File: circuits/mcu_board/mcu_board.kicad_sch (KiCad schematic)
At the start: 79 parts, among them J1 USB_B_Micro, J2 Conn_01x13_Pin, J3 Conn_01x04_Pin, J4 Conn_01x03_Socket, SW1 SW_Push, SW10 SW_Push, SW11 SW_Push, SW12 SW_Push, SW13 SW_Push, SW2 SW_Push, SW3 SW_Push, SW4 SW_Push, SW5 SW_Push, SW6 SW_Push, SW7 SW_Push, SW8 SW_Push, SW9 SW_Push, U1 AMS1117-3.3, U2 74HC165, U3 74HC165, U4 STM32F302CCTx, Y1 8MHz

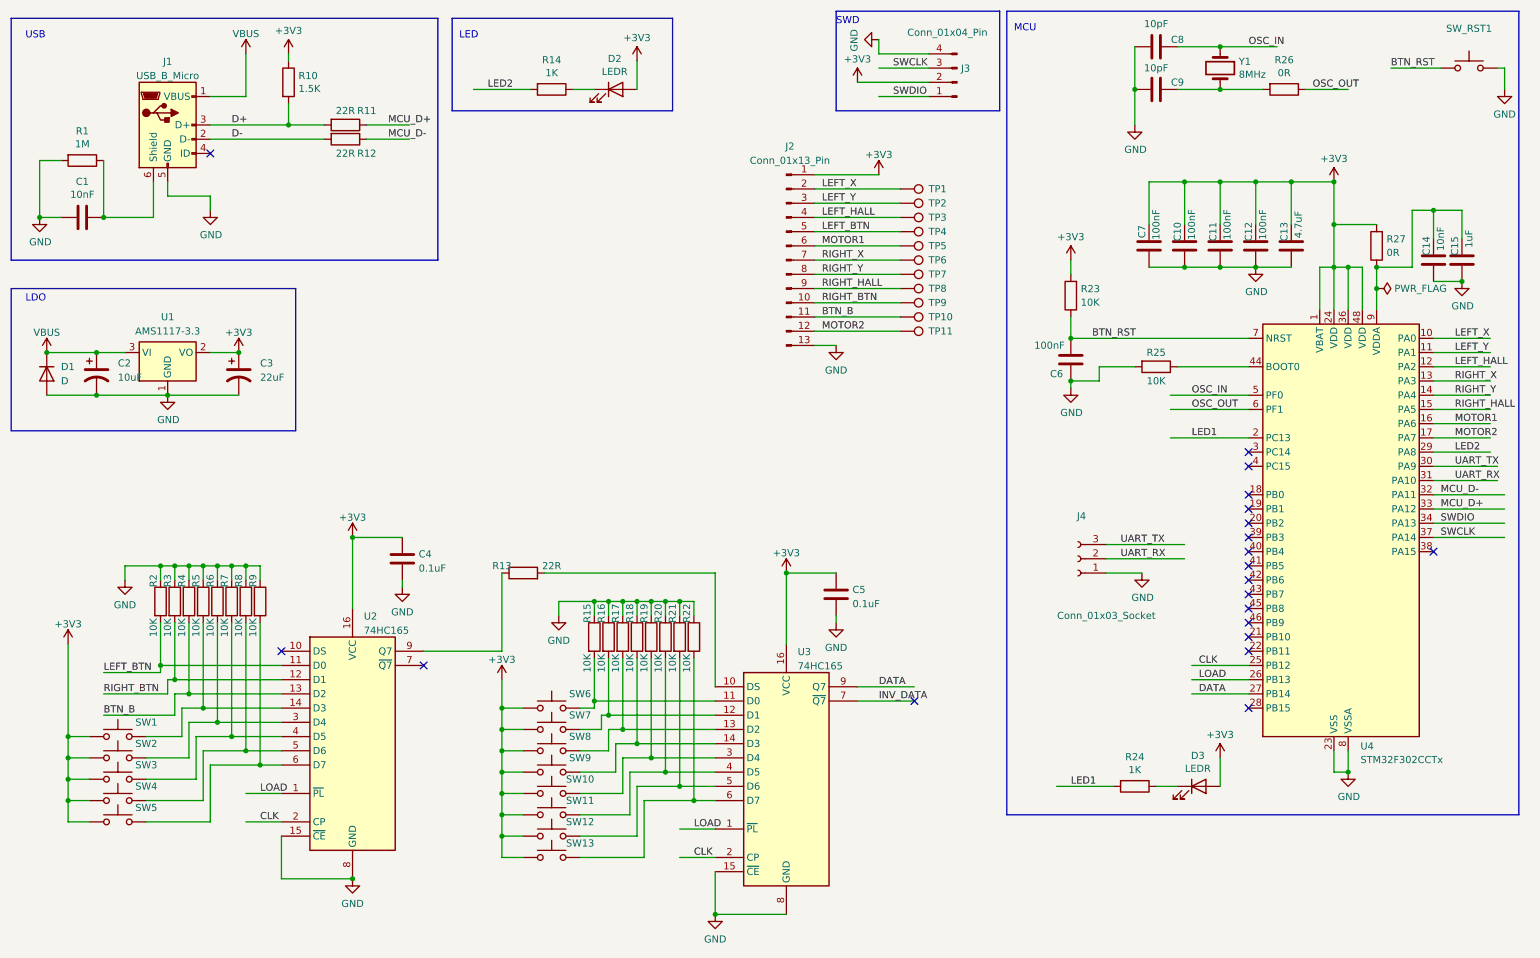
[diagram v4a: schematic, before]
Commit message: 更新mcu板原理图,改晶振封装
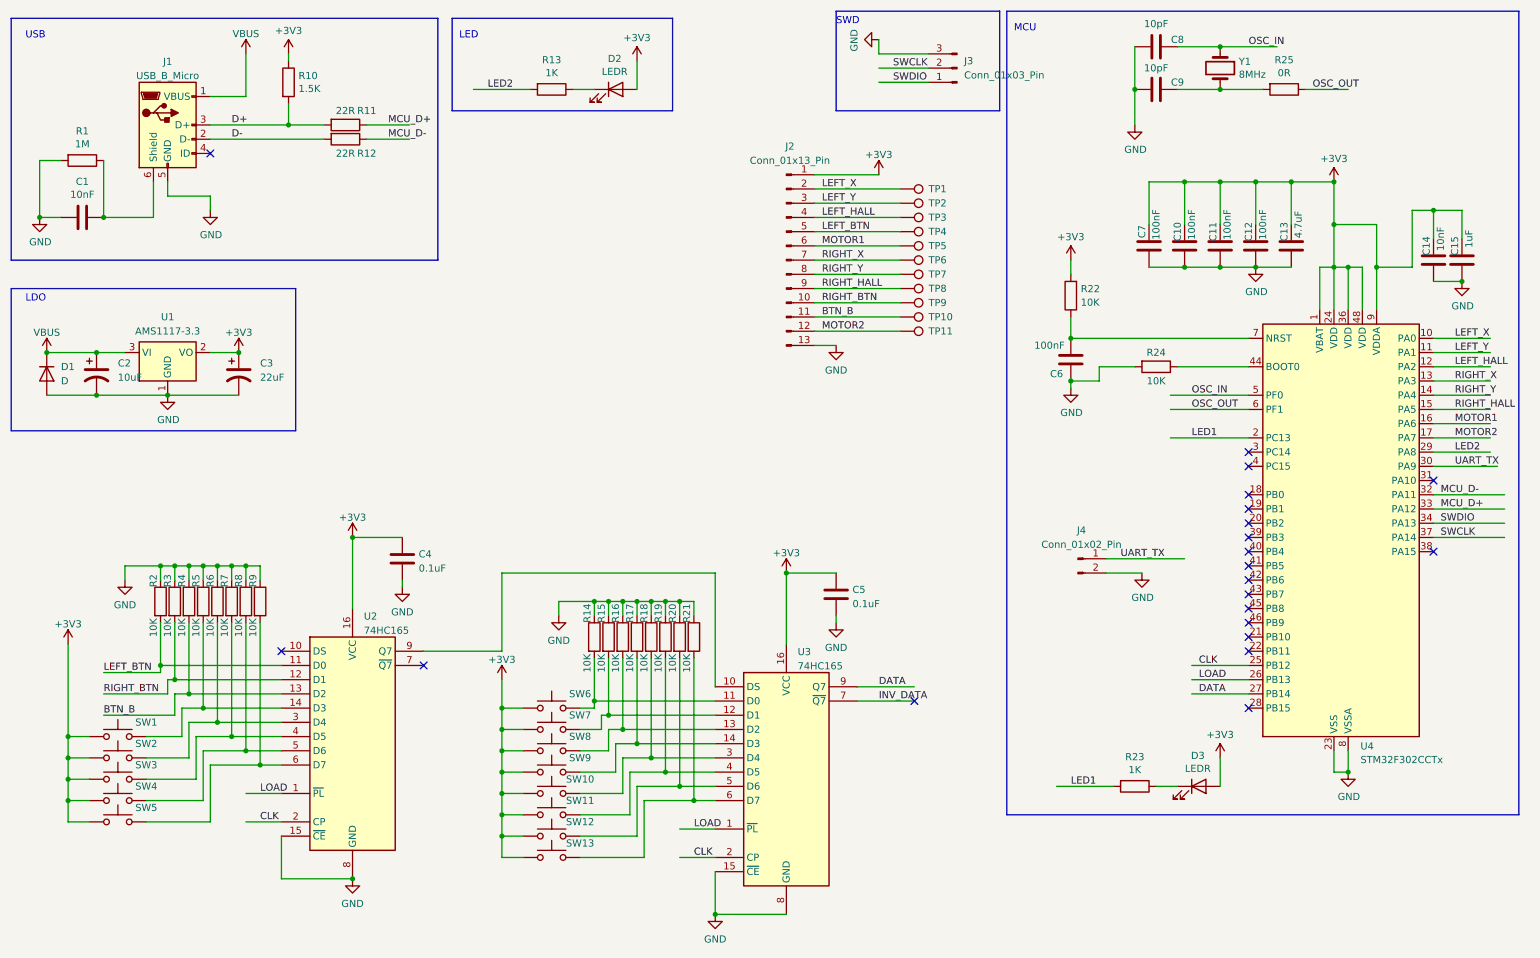
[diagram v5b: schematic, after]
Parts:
- removed J3: Conn_01x04_Pin, Connector_PinSocket_2.54mm:PinSocket_1x04_P2.54mm_Vertical, symbol Connector:Conn_01x04_Pin
- removed J4: Conn_01x03_Socket, Connector_PinSocket_2.54mm:PinSocket_1x03_P2.54mm_Vertical, symbol Connector:Conn_01x03_Socket
- removed R13: 22R, Resistor_SMD:R_0805_2012Metric_Pad1.20x1.40mm_HandSolder, symbol Device:R
- removed R27: 0R, Resistor_SMD:R_0805_2012Metric_Pad1.20x1.40mm_HandSolder, symbol Device:R
- removed SW_RST1: SW_RST, Button_Switch_SMD:SW_Push_1P1T_NO_6x6mm_H9.5mm, symbol Switch:SW_Push
- added J3: Conn_01x03_Pin, Connector_PinHeader_2.54mm:PinHeader_1x03_P2.54mm_Vertical, symbol Connector:Conn_01x03_Pin
- added J4: Conn_01x02_Pin, Connector_PinHeader_2.54mm:PinHeader_1x02_P2.54mm_Vertical, symbol Connector:Conn_01x02_Pin
- Y1: footprint Crystal:Crystal_SMD_HC49-SD_HandSoldering -> Crystal:Crystal_SMD_5032-2Pin_5.0x3.2mm_HandSoldering
- renumbered R14 to R13, R15 to R14, R16 to R15, R17 to R16, R18 to R17, R19 to R18, R20 to R19, R21 to R20, R22 to R21, R23 to R22, R24 to R23, R25 to R24, R26 to R25
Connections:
- net +3V3: now also C14.1, C15.1, U4.9 (VDDA)
- net GND: now also J3.3 (Pin_3), J4.2 (Pin_2)
- net SWCLK: now also J3.2 (Pin_2)
- net SWDIO: now also J3.1 (Pin_1)
- net UART_TX: now also J4.1 (Pin_1)
- net at U3.10 (DS): now also U2.9 (Q7)
- net BTN_RST: no longer names the net of C6.1, R22.1, U4.7 (NRST)
- net UART_RX: no longer names the net of U4.31 (PA10)
- no-connect marks 20 -> 21

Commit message: mcu板极端精简电路
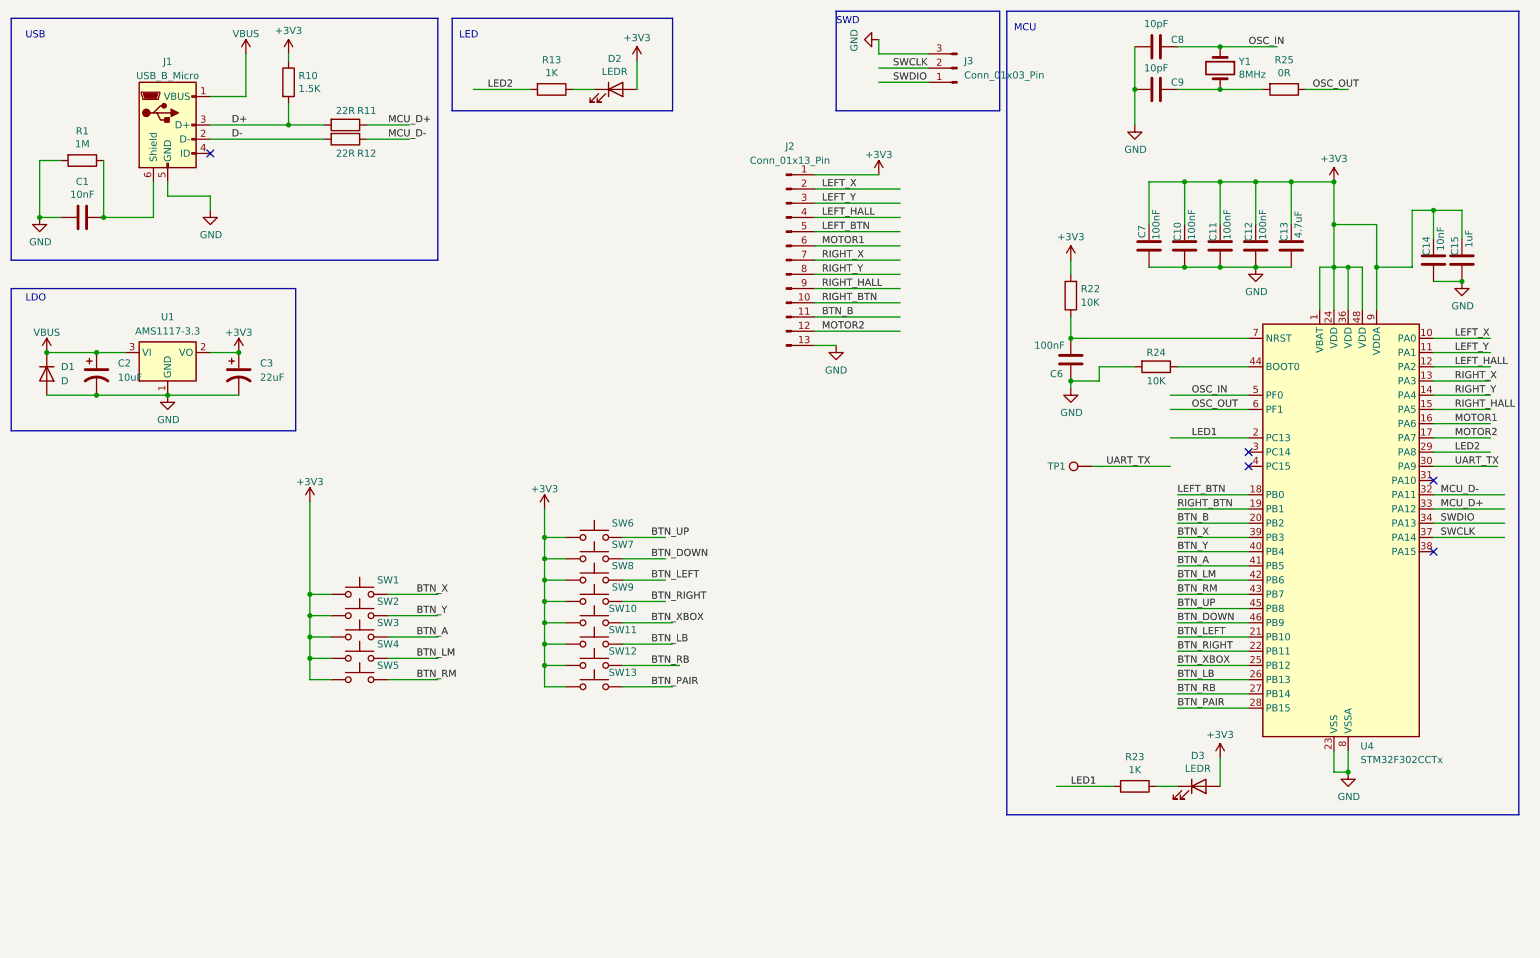
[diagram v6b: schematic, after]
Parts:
- removed C4, C5: 0.1uF, Capacitor_SMD:C_0805_2012Metric_Pad1.18x1.45mm_HandSolder, symbol Device:C
- removed J4: Conn_01x02_Pin, Connector_PinHeader_2.54mm:PinHeader_1x02_P2.54mm_Vertical, symbol Connector:Conn_01x02_Pin
- removed R14, R15, R16, R17, R18, R19, R2, R20, R21, R3, R4, R5, R6, R7, R8, R9: 10K, Resistor_SMD:R_0805_2012Metric_Pad1.20x1.40mm_HandSolder, symbol Device:R
- removed TP10, TP11, TP2, TP3, TP4, TP5, TP6, TP7, TP8, TP9: TestPoint, TestPoint:TestPoint_Pad_1.5x1.5mm, symbol Connector:TestPoint
- removed U2, U3: 74HC165, Package_SO:SOP-16_4.4x10.4mm_P1.27mm, symbol 74xx:74HC165
- TP1: footprint TestPoint:TestPoint_Pad_1.5x1.5mm -> TestPoint:TestPoint_Pad_1.0x1.0mm
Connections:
- net CLK is gone; now on net BTN_XBOX: U4.25 (PB12)
- net DATA is gone; now on net BTN_RB: U4.27 (PB14)
- net LOAD is gone; now on net BTN_LB: U4.26 (PB13)
- net BTN_B: now also U4.20 (PB2)
- net LEFT_BTN: now also U4.18 (PB0)
- net LEFT_X: no longer TP1.1
- net RIGHT_BTN: now also U4.19 (PB1)
- net UART_TX: now also TP1.1
- net BTN_PAIR: now reaches SW13.2
- net BTN_PAIR: now also U4.28 (PB15)
- net BTN_A: now reaches SW3.2
- net BTN_A: now also U4.41 (PB5)
- net BTN_Y: now reaches SW2.2
- net BTN_Y: now also U4.40 (PB4)
- net BTN_XBOX: now reaches SW10.2
- net BTN_X: now reaches SW1.2
- net BTN_X: now also U4.39 (PB3)
- net BTN_UP: now reaches SW6.2
- net BTN_UP: now also U4.45 (PB8)
- net BTN_DOWN: now reaches SW7.2
- net BTN_DOWN: now also U4.46 (PB9)
- net BTN_LEFT: now reaches SW8.2
- net BTN_LEFT: now also U4.21 (PB10)
- net BTN_RIGHT: now reaches SW9.2
- net BTN_RIGHT: now also U4.22 (PB11)
- net BTN_LB: now reaches SW11.2
- net BTN_RB: now reaches SW12.2
- net BTN_LM: now reaches SW4.2
- net BTN_LM: now also U4.42 (PB6)
- net BTN_RM: now reaches SW5.2
- net BTN_RM: now also U4.43 (PB7)
- no-connect marks 21 -> 5
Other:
- moved on the sheet: SW1, SW10, SW11, SW12, SW13, SW2, SW3, SW4, SW5, SW6, SW7, SW8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

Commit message: laytou MCU板基本完成走线
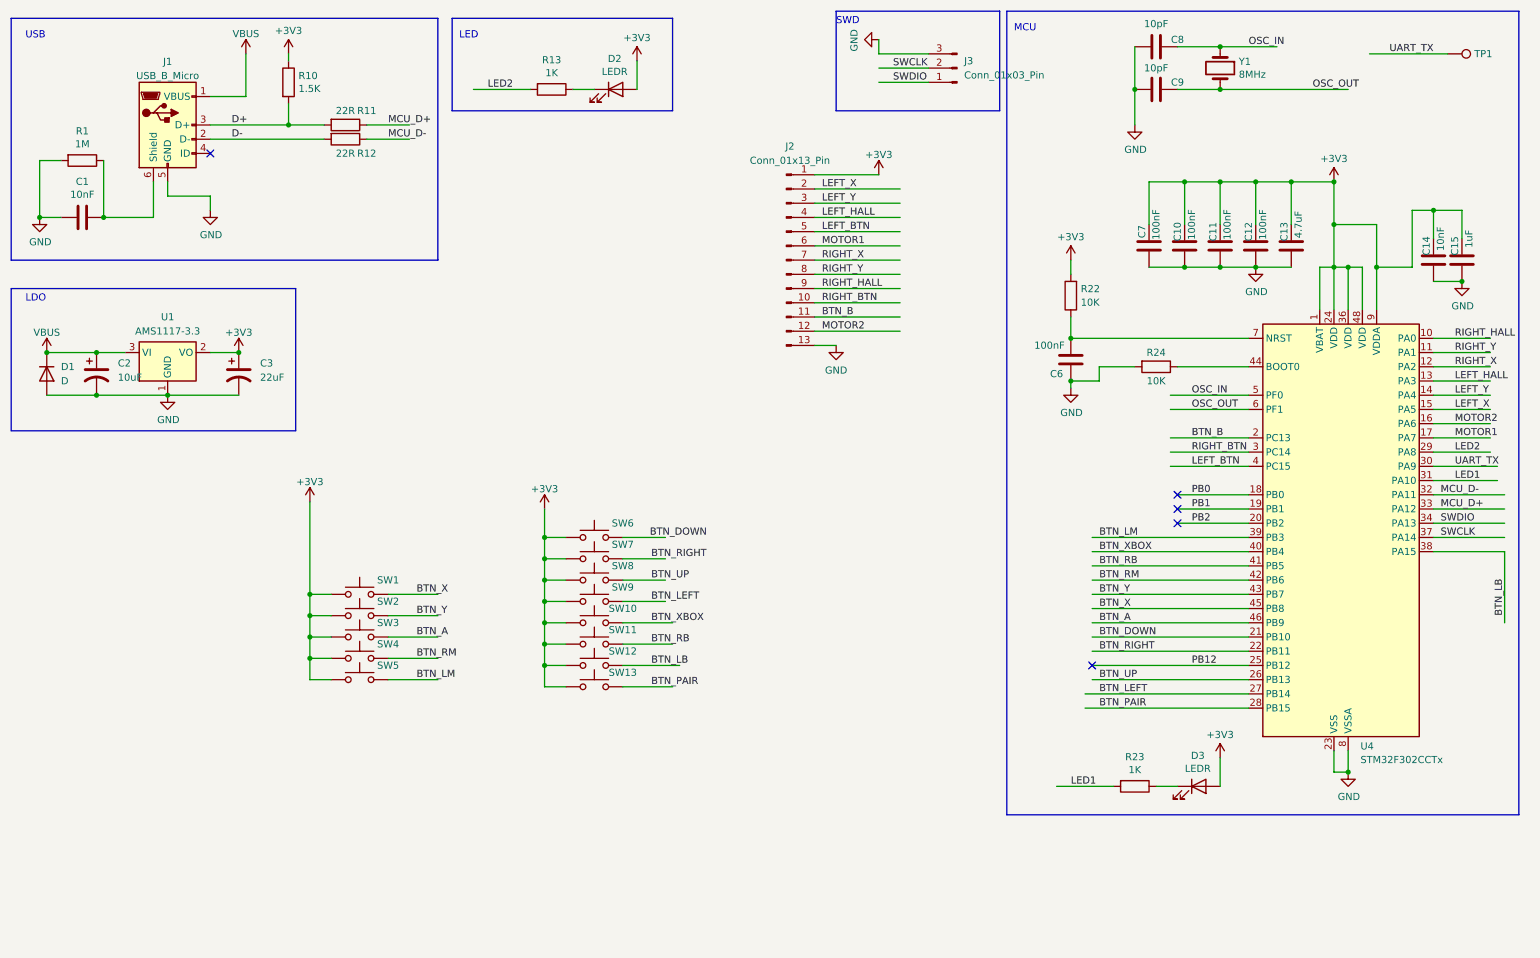
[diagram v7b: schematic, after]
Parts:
- removed R25: 0R, Resistor_SMD:R_0805_2012Metric_Pad1.20x1.40mm_HandSolder, symbol Device:R
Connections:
- net BTN_A: now also U4.46 (PB9); no longer U4.41 (PB5)
- net BTN_B: now also U4.2 (PC13); no longer U4.20 (PB2)
- net BTN_DOWN: now also SW6.2, U4.21 (PB10); no longer SW7.2, U4.46 (PB9)
- net BTN_LB: now also SW12.2, U4.38 (PA15); no longer SW11.2, U4.26 (PB13)
- net BTN_LEFT: now also SW9.2, U4.27 (PB14); no longer SW8.2, U4.21 (PB10)
- net BTN_LM: now also SW5.2, U4.39 (PB3); no longer SW4.2, U4.42 (PB6)
- net BTN_RB: now also SW11.2, U4.41 (PB5); no longer SW12.2, U4.27 (PB14)
- net BTN_RIGHT: now also SW7.2; no longer SW9.2
- net BTN_RM: now also SW4.2, U4.42 (PB6); no longer SW5.2, U4.43 (PB7)
- net BTN_UP: now also SW8.2, U4.26 (PB13); no longer SW6.2, U4.45 (PB8)
- net BTN_X: now also U4.45 (PB8); no longer U4.39 (PB3)
- net BTN_XBOX: now also U4.40 (PB4); no longer U4.25 (PB12)
- net BTN_Y: now also U4.43 (PB7); no longer U4.40 (PB4)
- net LED1: now also U4.31 (PA10); no longer U4.2 (PC13)
- net LEFT_BTN: now also U4.4 (PC15); no longer U4.18 (PB0)
- net LEFT_HALL: now also U4.13 (PA3); no longer U4.12 (PA2)
- net LEFT_X: now also U4.15 (PA5); no longer U4.10 (PA0)
- net LEFT_Y: now also U4.14 (PA4); no longer U4.11 (PA1)
- net MOTOR1: now also U4.17 (PA7); no longer U4.16 (PA6)
- net MOTOR2: now also U4.16 (PA6); no longer U4.17 (PA7)
- net OSC_OUT: now also C9.1, Y1.2
- net RIGHT_BTN: now also U4.3 (PC14); no longer U4.19 (PB1)
- net RIGHT_HALL: now also U4.10 (PA0); no longer U4.15 (PA5)
- net RIGHT_X: now also U4.12 (PA2); no longer U4.13 (PA3)
- net RIGHT_Y: now also U4.11 (PA1); no longer U4.14 (PA4)
- new net PB0: U4.18 (PB0)
- new net PB1: U4.19 (PB1)
- new net PB12: U4.25 (PB12)
- new net PB2: U4.20 (PB2)

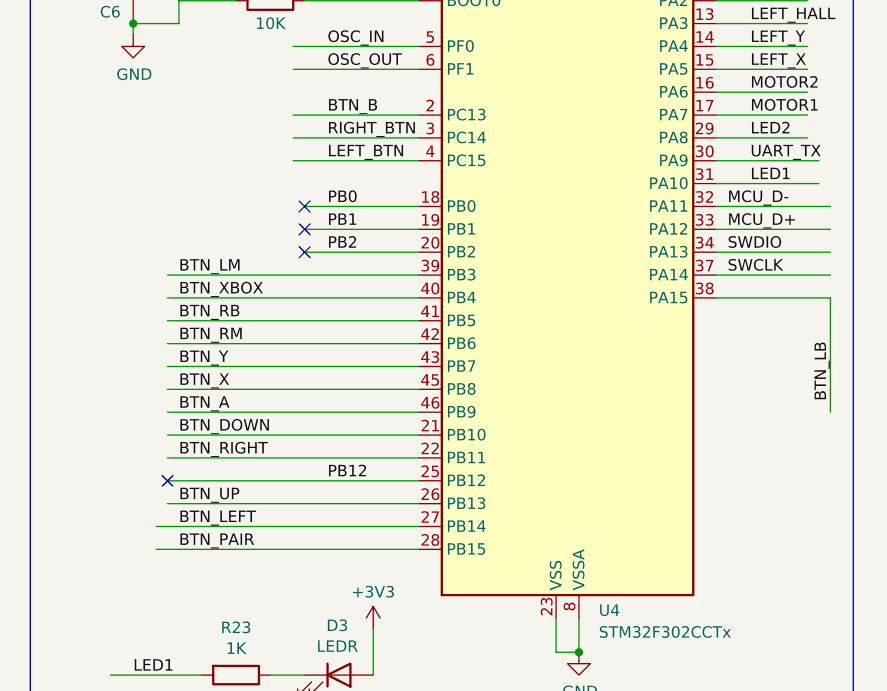
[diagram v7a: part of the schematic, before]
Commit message: 按键逻辑修改完成,未测试
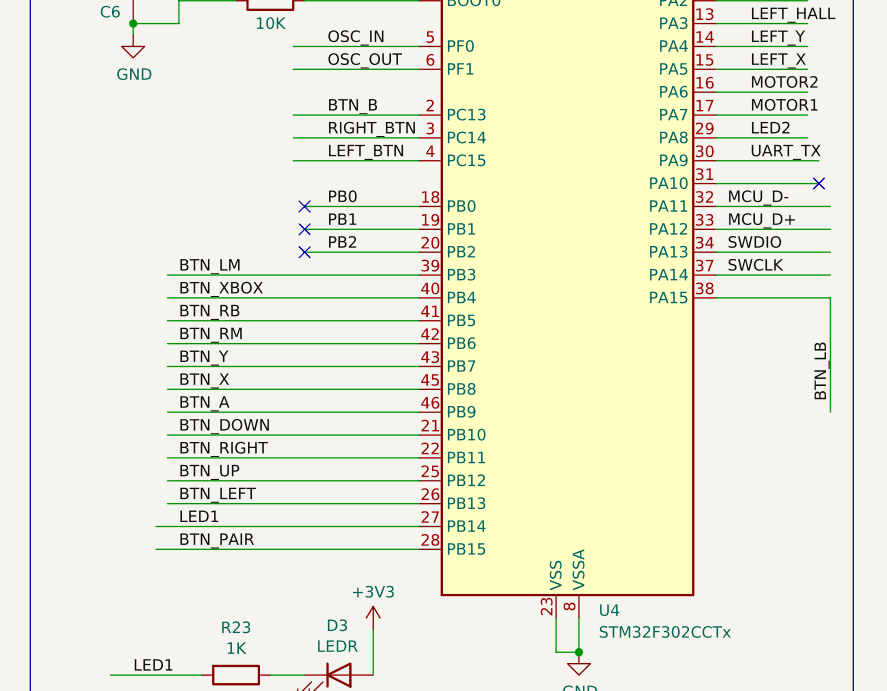
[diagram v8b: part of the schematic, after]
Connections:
- net PB12 is gone; now on net BTN_UP: U4.25 (PB12)
- net BTN_LEFT: now also U4.26 (PB13); no longer U4.27 (PB14)
- net BTN_UP: no longer U4.26 (PB13)
- net LED1: now also U4.27 (PB14); no longer U4.31 (PA10)
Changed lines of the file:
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@@
   (no_connect (at 50.8 38.1))
   (no_connect (at 223.52 99.06))
-  (no_connect (at 208.28 129.54))
   (no_connect (at 223.52 104.14))
   (no_connect (at 223.52 101.6))
+  (no_connect (at 280.67 96.52))
   (wire (pts (xy 237.49 43.18) (xy 237.49 50.8))
     (stroke (width 0) (type default))
@@
     (effects (font (size 1.27 1.27)) (justify left bottom))
   )
-  (label "BTN_LEFT" (at 209.55 134.62 0) (fields_autoplaced)
-    (effects (font (size 1.27 1.27)) (justify left bottom))
-  )
   (label "BTN_A" (at 87.63 124.46 0) (fields_autoplaced)
-    (effects (font (size 1.27 1.27)) (justify left bottom))
-  )
-  (label "PB12" (at 226.06 129.54 0) (fields_autoplaced)
     (effects (font (size 1.27 1.27)) (justify left bottom))
   )
@@
     (effects (font (size 1.27 1.27)) (justify left bottom))
   )
+  (label "BTN_LEFT" (at 209.55 132.08 0) (fields_autoplaced)
+    (effects (font (size 1.27 1.27)) (justify left bottom))
+  )
   (label "BTN_PAIR" (at 209.55 137.16 0) (fields_autoplaced)
     (effects (font (size 1.27 1.27)) (justify left bottom))
   )
+  (label "BTN_UP" (at 209.55 129.54 0) (fields_autoplaced)
+    (effects (font (size 1.27 1.27)) (justify left bottom))
+  )
   (label "SWCLK" (at 270.51 106.68 0) (fields_autoplaced)
     (effects (font (size 1.27 1.27)) (justify left bottom))
@@
     (effects (font (size 1.27 1.27)) (justify left bottom))
   )
-  (label "LED1" (at 273.05 96.52 0) (fields_autoplaced)
+  (label "LED1" (at 209.55 134.62 0) (fields_autoplaced)
     (effects (font (size 1.27 1.27)) (justify left bottom))
   )
@@
     (effects (font (size 1.27 1.27)) (justify left bottom))
   )
-  (label "BTN_UP" (at 209.55 132.08 0) (fields_autoplaced)
-    (effects (font (size 1.27 1.27)) (justify left bottom))
-  )
